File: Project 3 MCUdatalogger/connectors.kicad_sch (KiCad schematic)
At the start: 4 parts, among them J1 Conn_01x04_Pin, J2 Conn_01x04_Pin, J3 Conn_01x09_Pin, J4 Conn_02x03_Odd_Even

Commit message: Completed Symbol to footprint associations
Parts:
- J1, J2: footprint (none) -> Connector_PinHeader_2.54mm:PinHeader_1x04_P2.54mm_Vertical
- J3: footprint (none) -> Connector_PinHeader_2.54mm:PinHeader_1x09_P2.54mm_Vertical
- J4: footprint (none) -> Connector_PinHeader_2.54mm:PinHeader_2x03_P2.54mm_Vertical
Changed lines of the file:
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@@
 			)
 		)
-		(property "Footprint" ""
+		(property "Footprint" "Connector_PinHeader_2.54mm:PinHeader_2x03_P2.54mm_Vertical"
 			(at 93.345 100.965 0)
 			(effects
@@
 			)
 		)
-		(property "Footprint" ""
+		(property "Footprint" "Connector_PinHeader_2.54mm:PinHeader_1x04_P2.54mm_Vertical"
 			(at 92.71 77.47 0)
 			(effects
@@
 			)
 		)
-		(property "Footprint" ""
+		(property "Footprint" "Connector_PinHeader_2.54mm:PinHeader_1x09_P2.54mm_Vertical"
 			(at 73.025 107.315 0)
 			(effects
@@
 			)
 		)
-		(property "Footprint" ""
+		(property "Footprint" "Connector_PinHeader_2.54mm:PinHeader_1x04_P2.54mm_Vertical"
 			(at 73.66 77.47 0)
 			(effects

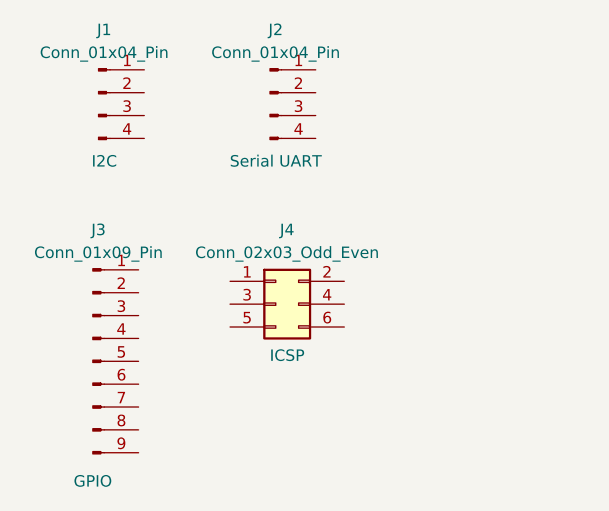
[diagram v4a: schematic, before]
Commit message: Completed wiring in the second sheet.
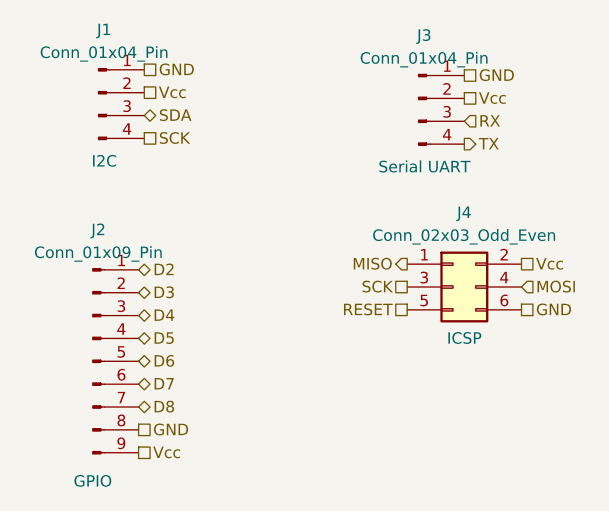
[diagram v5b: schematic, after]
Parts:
- renumbered J3 to J2, J2 to J3
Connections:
- net MISO: now reaches J4.1 (Pin_1)
- net Vcc: now reaches J4.2 (Pin_2)
- net Vcc: now also J1.2 (Pin_2), J2.9 (Pin_9), J3.2 (Pin_2)
- net SCK: now reaches J4.3 (Pin_3)
- net SCK: now also J1.4 (Pin_4)
- net MOSI: now reaches J4.4 (Pin_4)
- net RESET: now reaches J4.5 (Pin_5)
- net GND: now reaches J4.6 (Pin_6)
- net GND: now also J1.1 (Pin_1), J2.8 (Pin_8), J3.1 (Pin_1)
- net RX: now reaches J3.3 (Pin_3)
- net TX: now reaches J3.4 (Pin_4)
- net D2: now reaches J2.1 (Pin_1)
- net D3: now reaches J2.2 (Pin_2)
- net D4: now reaches J2.3 (Pin_3)
- net D5: now reaches J2.4 (Pin_4)
- net D6: now reaches J2.5 (Pin_5)
- net D7: now reaches J2.6 (Pin_6)
- net D8: now reaches J2.7 (Pin_7)
- net SDA: now reaches J1.3 (Pin_3)
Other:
- moved on the sheet: J3, J4

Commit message: Completed Comments
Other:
- moved on the sheet: J1
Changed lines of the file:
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@@
 	(hierarchical_label "SCK"
 		(shape passive)
-		(at 78.74 82.55 0)
+		(at 78.74 83.82 0)
 		(fields_autoplaced yes)
 		(effects
@@
 	(hierarchical_label "SDA"
 		(shape bidirectional)
-		(at 78.74 80.01 0)
+		(at 78.74 81.28 0)
 		(fields_autoplaced yes)
 		(effects
@@
 	(hierarchical_label "Vcc"
 		(shape passive)
-		(at 78.74 77.47 0)
+		(at 78.74 78.74 0)
 		(fields_autoplaced yes)
 		(effects
@@
 	(hierarchical_label "GND"
 		(shape passive)
-		(at 78.74 74.93 0)
+		(at 78.74 76.2 0)
 		(fields_autoplaced yes)
 		(effects
@@
 	(symbol
 		(lib_id "Connector:Conn_01x04_Pin")
-		(at 73.66 77.47 0)
+		(at 73.66 78.74 0)
 		(unit 1)
 		(exclude_from_sim no)
@@
 		(dnp no)
 		(property "Reference" "J1"
-			(at 74.295 70.485 0)
+			(at 74.295 71.755 0)
 			(effects
 				(font
@@
 		)
 		(property "Value" "Conn_01x04_Pin"
-			(at 74.295 73.025 0)
+			(at 74.295 74.295 0)
 			(effects
 				(font
@@
 		)
 		(property "Footprint" "Connector_PinHeader_2.54mm:PinHeader_1x04_P2.54mm_Vertical"
-			(at 73.66 77.47 0)
+			(at 73.66 78.74 0)
 			(effects
 				(font
@@
 		)
 		(property "Datasheet" "~"
-			(at 73.66 77.47 0)
+			(at 73.66 78.74 0)
 			(effects
 				(font
@@
 		)
 		(property "Description" "Generic connector, single row, 01x04, script generated"
-			(at 73.66 77.47 0)
+			(at 73.66 78.74 0)
 			(effects
 				(font
@@
 		)
 		(property "Purpose" "I2C"
-			(at 74.295 85.09 0)
-			(effects
-				(font
+			(at 74.295 86.36 0)
+			(effects
+				(font
